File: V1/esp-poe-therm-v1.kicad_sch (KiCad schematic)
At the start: 48 parts, among them J1 USB_C_Receptacle_USB2.0, J2 RJ45 JACK, J3 PT1000 RTD, Q1 UMH3N, Q2 WPM2015-3/TR, Q3 LMUN2211LT1G, SW1 RESET, U4 CH340C, U5 ESP32-WROOM-32E-N4, U6 LAN8710A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

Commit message: Lots of stuff
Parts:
- R25: value 4,02k/100mW -> 4,02k/62,5mW; footprint Tales:R_0603_1608Metric -> Tales:R_0402_1005Metric; Case 0603/1608 -> (none); LCSC Part # C705863 -> C852810; Mfr PN RT0603BRE074K02L -> RT0402BRD074K02L; Package (none) -> 0402/1005; Vendor PN C705863 -> C852810
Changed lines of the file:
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@@
 			)
 		)
-		(property "Value" "4,02k/100mW"
+		(property "Value" "4,02k/62,5mW"
 			(at 177.8 222.25 0)
 			(effects
@@
 			)
 		)
-		(property "Footprint" "Tales:R_0603_1608Metric"
+		(property "Footprint" "Tales:R_0402_1005Metric"
 			(at 176.276 222.504 90)
 			(effects
@@
 			)
 		)
-		(property "Case" "0603/1608"
+		(property "Case" ""
 			(at 175.26 222.25 0)
 			(effects
@@
 			)
 		)
-		(property "Mfr PN" "RT0603BRE074K02L"
+		(property "Mfr PN" "RT0402BRD074K02L"
 			(at 175.26 222.25 0)
 			(effects
@@
 			)
 		)
-		(property "Vendor PN" "C705863"
+		(property "Vendor PN" "C852810"
 			(at 175.26 222.25 0)
 			(effects
@@
 			)
 		)
-		(property "LCSC Part #" "C705863"
+		(property "LCSC Part #" "C852810"
 			(at 177.8 227.33 0)
 			(effects
@@
 			(at 175.26 222.25 0)
 			(effects
+				(font
+					(size 1.27 1.27)
+				)
+				(hide yes)
+			)
+		)
+		(property "Package" "0402/1005"
+			(at 175.26 222.25 0)
+			(effects

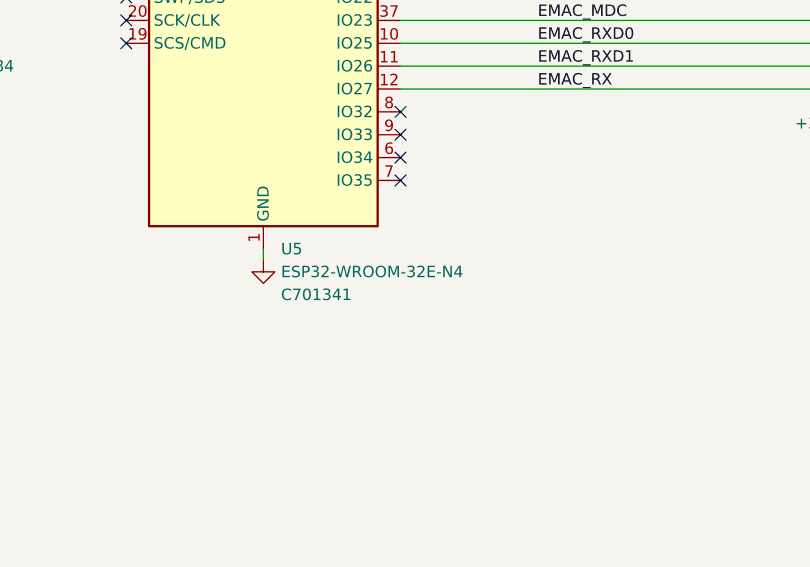
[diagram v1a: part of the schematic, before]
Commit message: Replace ESP32 for externa antena version
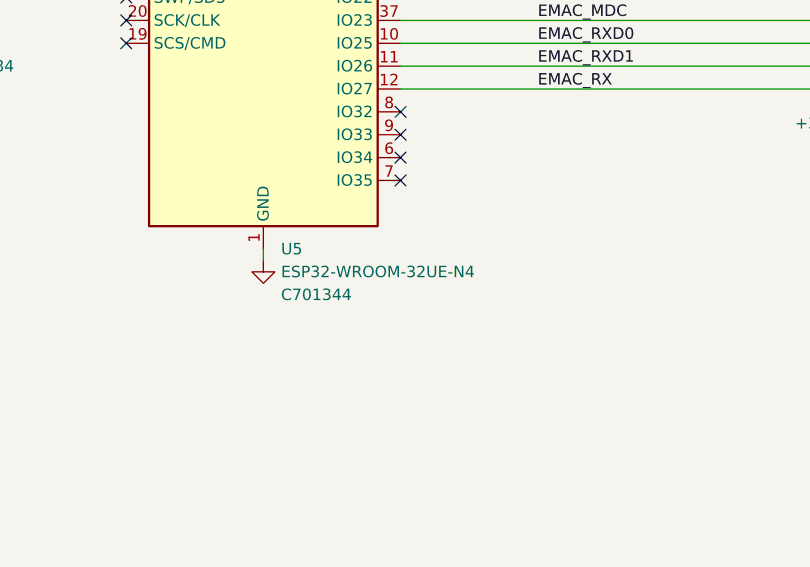
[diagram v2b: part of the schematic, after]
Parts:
- U5: value ESP32-WROOM-32E-N4 -> ESP32-WROOM-32UE-N4; footprint Tales:ESP32-WROOM-32 -> Tales:ESP32-WROOM-32U; LCSC Part # C701341 -> C701344; Vendor PN C701341 -> C701344
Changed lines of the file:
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@@
 			)
 		)
-		(property "Value" "ESP32-WROOM-32E-N4"
+		(property "Value" "ESP32-WROOM-32UE-N4"
 			(at 183.5659 133.35 0)
 			(effects
@@
 			)
 		)
-		(property "Footprint" "Tales:ESP32-WROOM-32"
+		(property "Footprint" "Tales:ESP32-WROOM-32U"
 			(at 181.61 133.35 0)
 			(effects
@@
 			)
 		)
-		(property "LCSC Part #" "C701341"
+		(property "LCSC Part #" "C701344"
 			(at 183.5659 135.89 0)
 			(effects
@@
 			)
 		)
-		(property "Vendor PN" "C701341"
+		(property "Vendor PN" "C701344"
 			(at 181.61 95.25 0)
 			(effects

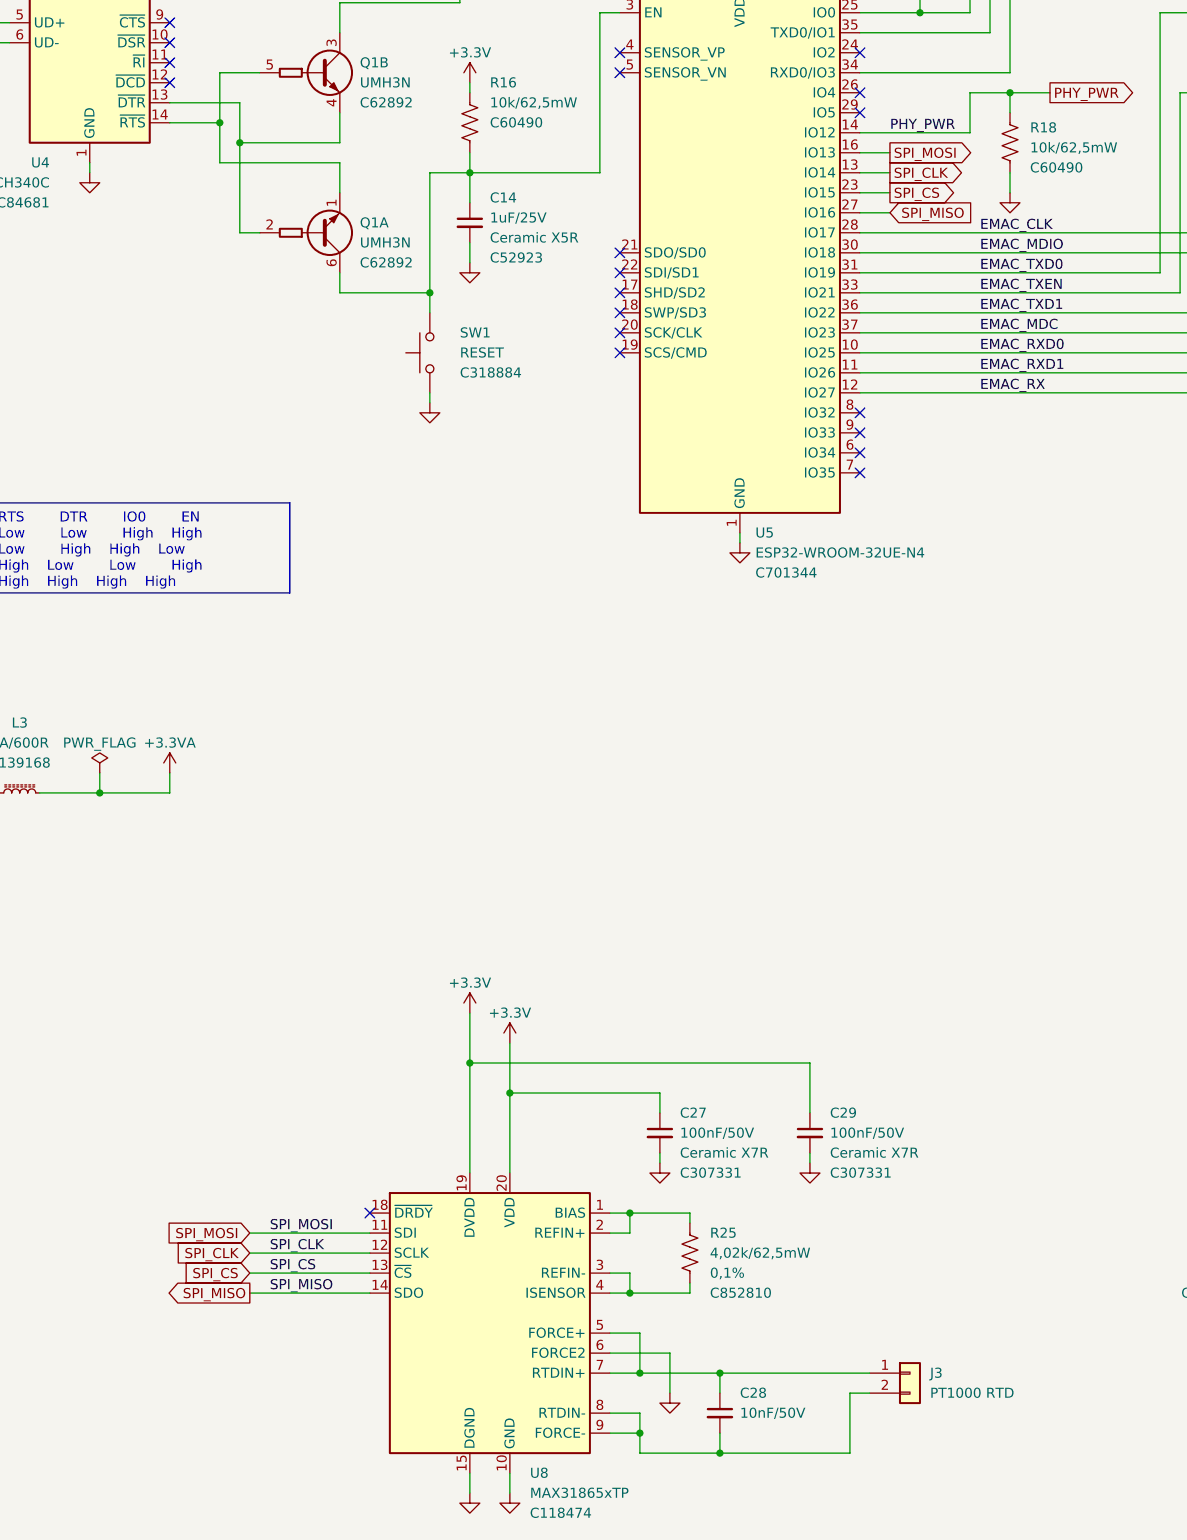
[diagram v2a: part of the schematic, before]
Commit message: Replace sensor type
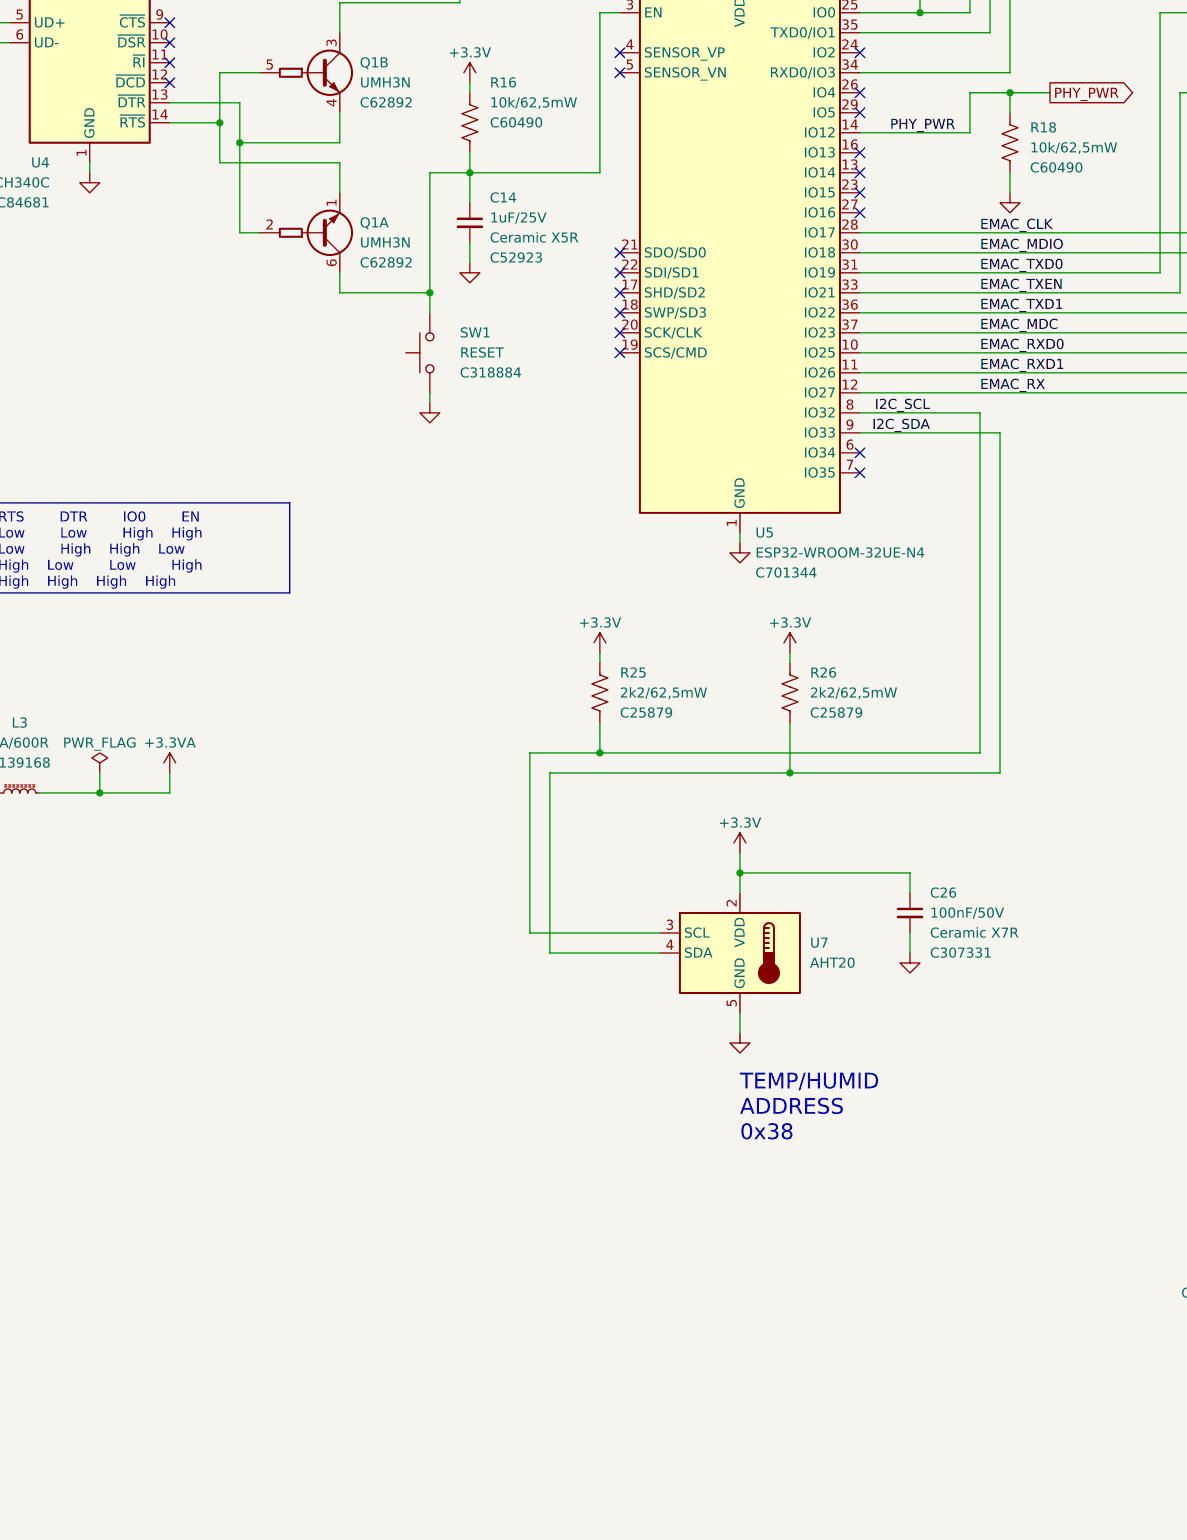
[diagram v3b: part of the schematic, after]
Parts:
- removed C27, C29: 100nF/50V, Tales:C_0402_1005Metric, symbol Device:C_Small
- removed C28: 10nF/50V, Tales:C_0402_1005Metric, symbol Device:C_Small
- removed J3: PT1000 RTD, Tales:TerminalBlock_Dibo_DB141R-2.54-2P_1x02_P2.54mm_Horizontal, symbol Connector_Generic:Conn_01x02
- removed U8: MAX31865xTP, Tales:TQFN-20-1EP_5x5mm_P0.65mm_EP3.25x3.25mm_ThermalVias, symbol Sensor_Temperature:MAX31865xTP
- added C26: 100nF/50V, Tales:C_0402_1005Metric, symbol Device:C_Small
- added R26: 2k2/62,5mW, Tales:R_0402_1005Metric, symbol Device:R_US
- added U7: AHT20, Tales:DFN-6-3x3mm_P1mm, symbol Tales:AHT20
- R25: value 4,02k/62,5mW -> 2k2/62,5mW; Case (none) -> 0402/1005; LCSC Part # C852810 -> C25879; Mfr YAGEO -> Uniroyal; Mfr PN RT0402BRD074K02L -> 0402WGF2201TCE; Package 0402/1005 -> (none); Technology 0,1% -> (none); Vendor PN C852810 -> C25879
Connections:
- net +3.3V: now also R25.1, C26.1, R26.1, U7.2 (VDD)
- net GND: now also C26.2, U7.5 (GND)
- net I2C_SCL: now reaches U5.8 (IO32)
- net I2C_SCL: now also R25.2, U7.3 (SCL)
- net I2C_SDA: now reaches U5.9 (IO33)
- net I2C_SDA: now also R26.2, U7.4 (SDA)
- net SPI_CLK: no longer names the net of U5.13 (IO14)
- net SPI_CS: no longer names the net of U5.23 (IO15)
- net SPI_MISO: no longer names the net of U5.27 (IO16)
- net SPI_MOSI: no longer names the net of U5.16 (IO13)
- no-connect marks 28 -> 29
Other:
- note added: "TEMP/HUMID ADDRESS 0x38"

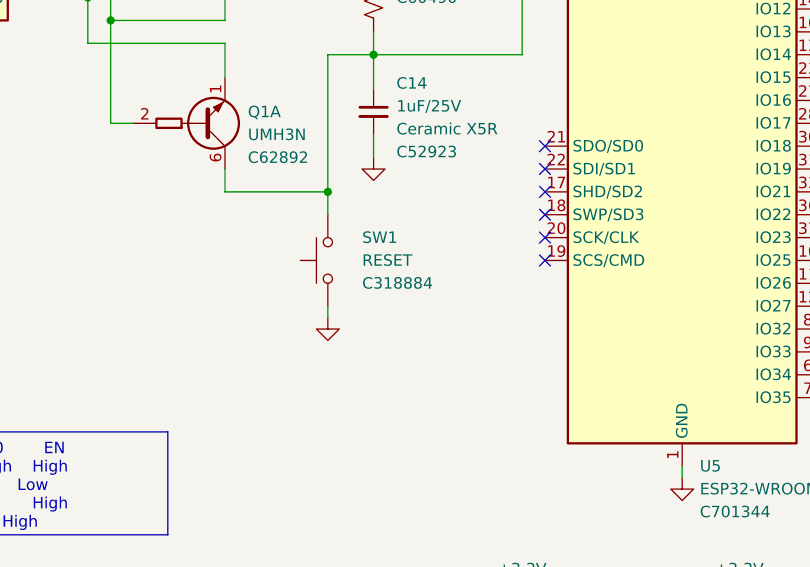
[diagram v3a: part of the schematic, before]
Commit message: Replacing external for onboard sensor
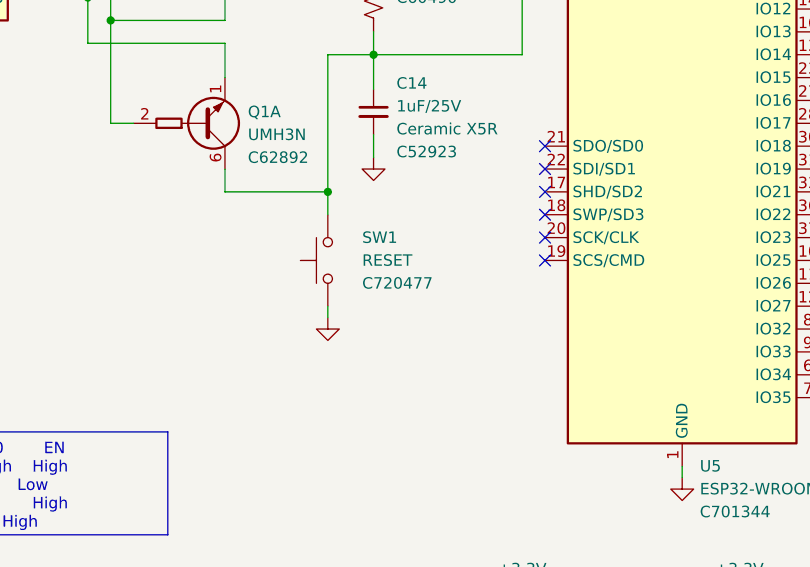
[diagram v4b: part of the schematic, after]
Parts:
- SW1: footprint Tales:SW_SPST_TL3342 -> Tales:SW_SPST_Xunpu_TS1088AR02016; LCSC Part # C318884 -> C720477; Mfr XKB Connectivity -> Xunpu; Mfr PN TS-1187A-B-A-B -> TS-1088-AR02016; Vendor PN C318884 -> C720477
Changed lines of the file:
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@@
 			)
 		)
-		(property "Footprint" "Tales:SW_SPST_TL3342"
+		(property "Footprint" "Tales:SW_SPST_Xunpu_TS1088AR02016"
 			(at 137.16 107.95 0)
 			(effects
@@
 			)
 		)
-		(property "LCSC Part #" "C318884"
+		(property "LCSC Part #" "C720477"
 			(at 146.05 110.4901 90)
 			(effects
@@
 			)
 		)
-		(property "Mfr" "XKB Connectivity"
+		(property "Mfr" "Xunpu"
 			(at 142.24 107.95 0)
 			(effects
@@
 			)
 		)
-		(property "Mfr PN" "TS-1187A-B-A-B"
+		(property "Mfr PN" "TS-1088-AR02016"
 			(at 142.24 107.95 0)
 			(effects
@@
 			)
 		)
-		(property "Vendor PN" "C318884"
+		(property "Vendor PN" "C720477"
 			(at 142.24 107.95 0)
 			(effects

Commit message: dev
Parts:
- added J3: Sensor Temperatura, Connector_JST:JST_PH_B4B-PH-K_1x04_P2.00mm_Vertical, symbol Connector_Generic:Conn_01x04
- added J4: Sensor Temperatura, Connector_JST:JST_PH_S4B-PH-K_1x04_P2.00mm_Horizontal, symbol Connector_Generic:Conn_01x04
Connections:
- net +3.3V: now also J3.1 (Pin_1); no longer C26.1, U7.2 (VDD)
- net GND: now also J3.4 (Pin_4); no longer C26.2, U7.5 (GND)
- net I2C_SCL: now also J3.2 (Pin_2); no longer U7.3 (SCL)
- net I2C_SDA: now also J3.3 (Pin_3); no longer U7.4 (SDA)
- new net: C26.2, J4.1 (Pin_1), U7.5 (GND)
- new net: J4.2 (Pin_2), U7.4 (SDA)
- new net: J4.3 (Pin_3), U7.3 (SCL)
- new net: C26.1, J4.4 (Pin_4), U7.2 (VDD)
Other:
- moved on the sheet: C26, U7
